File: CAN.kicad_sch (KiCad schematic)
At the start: 7 parts, among them U1 TCAN1462VDRQ1, U2 ESDCAN24-2BLY

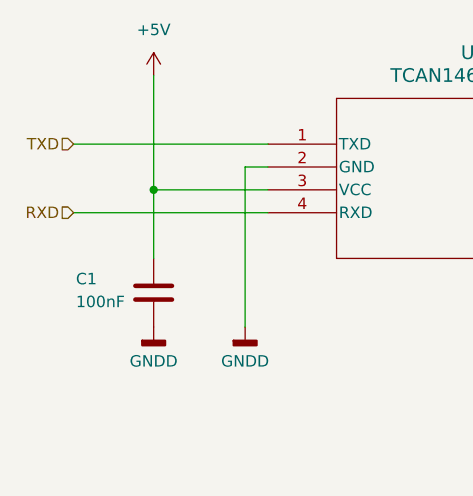
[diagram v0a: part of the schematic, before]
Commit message: fixed bcm connector, added thermistors something else too prolly
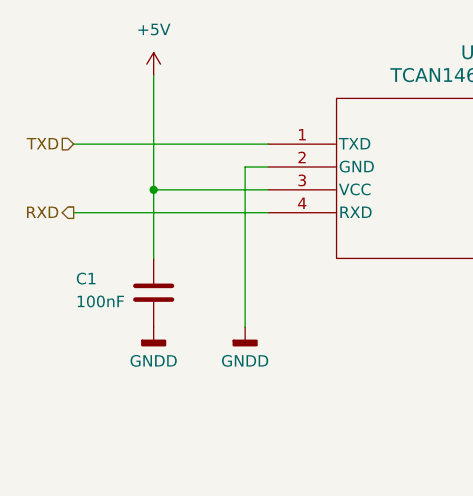
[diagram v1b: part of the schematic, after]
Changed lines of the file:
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@@
 	)
 	(hierarchical_label "RXD"
-		(shape input)
+		(shape output)
 		(at 73.66 95.25 180)
 		(effects
